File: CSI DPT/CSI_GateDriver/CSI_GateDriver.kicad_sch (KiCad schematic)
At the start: 0 parts

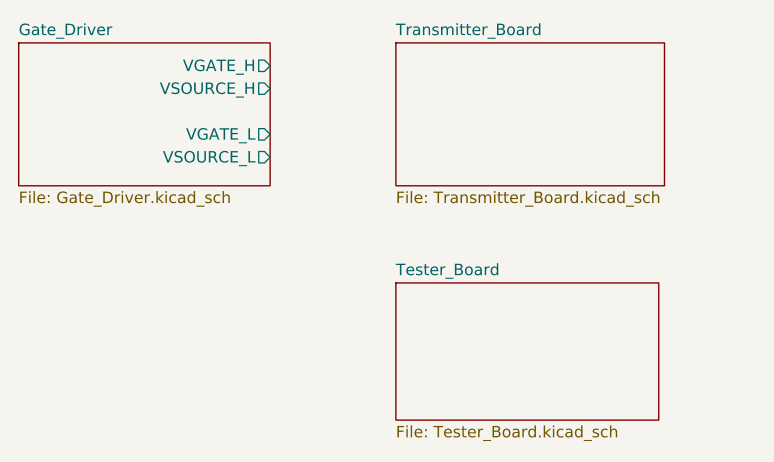
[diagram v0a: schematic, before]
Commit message: Picking up
1. Tidy up the project folders, one project split into two projects (gate driver + tester)
2. Gate driver PCB half way done
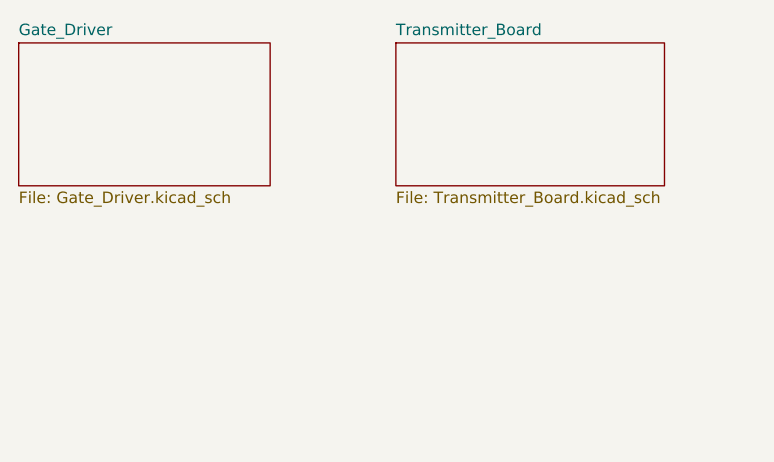
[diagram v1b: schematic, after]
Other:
- removed sheet Tester_Board
- sheet Gate_Driver ports: added none; removed VGATE_H, VGATE_L, VSOURCE_H, VSOURCE_L
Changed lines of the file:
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@@
 	(paper "A4")
-	(sheet
-		(at 73.66 60.96)
-		(size 29.21 15.24)
-		(exclude_from_sim no)
-		(in_bom yes)
-		(on_board yes)
-		(dnp no)
-		(fields_autoplaced yes)
-		(stroke
-			(width 0.1524)
-			(type solid)
-		)
-		(fill
-			(color 0 0 0 0.0000)
-		)
-		(property "Sheetname" "Tester_Board"
-			(at 73.66 60.2484 0)
-			(effects
-				(font
-					(size 1.27 1.27)
-				)
-				(justify left bottom)
-			)
-		)
-		(property "Sheetfile" "Tester_Board.kicad_sch"
-			(at 73.66 76.7846 0)
-			(effects
-				(font
-					(size 1.27 1.27)
-				)
-				(justify left top)
-			)
-		)
-		(instances
-			(project "CSI_DPT"
-				(path "/73752a49-eb43-43a5-aaa4-eec4feca9056"
-					(page "4")
-				)
-			)
-		)
-	)
 	(sheet
 		(at 31.75 34.29)
@@
 			)
 		)
-		(pin "VGATE_H" output
-			(at 59.69 36.83 0)
-			(effects
-				(font
-					(size 1.27 1.27)
-				)
-				(justify right)
-			)
-		)
-		(pin "VGATE_L" output
-			(at 59.69 44.45 0)
-			(effects
-				(font
-					(size 1.27 1.27)
-				)
-				(justify right)
-			)
-		)
-		(pin "VSOURCE_H" output
-			(at 59.69 39.37 0)
-			(effects
-				(font
-					(size 1.27 1.27)
-				)
-				(justify right)
-			)
-		)
-		(pin "VSOURCE_L" output
-			(at 59.69 46.99 0)
-			(effects
-				(font
-					(size 1.27 1.27)
-				)
-				(justify right)
-			)
-		)
 		(instances
-			(project "CSI_DPT"
+			(project "CSI_GateDriver"
 				(path "/73752a49-eb43-43a5-aaa4-eec4feca9056"
 					(page "2")
@@
 		)
 		(instances
-			(project "CSI_DPT"
+			(project "CSI_GateDriver"
 				(path "/73752a49-eb43-43a5-aaa4-eec4feca9056"
 					(page "3")
